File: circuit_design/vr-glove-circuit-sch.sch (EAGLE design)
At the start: 31 parts, among them U1 ARDUINO_SHIELDNO_SILK

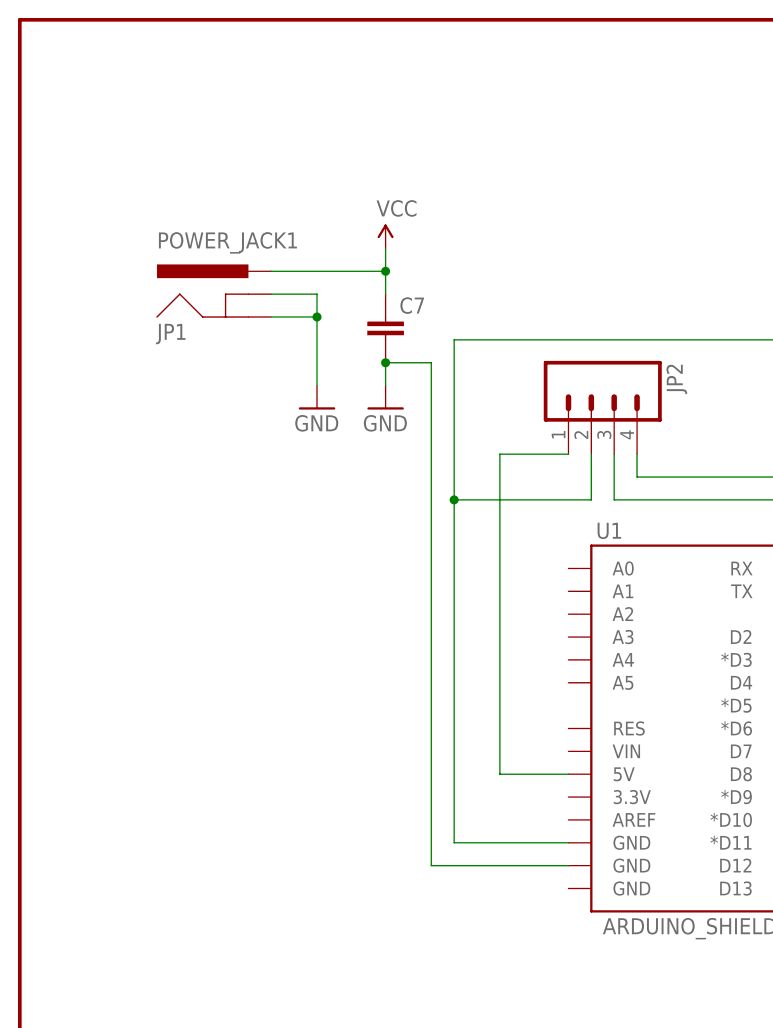
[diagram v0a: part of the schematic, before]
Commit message: added power supply
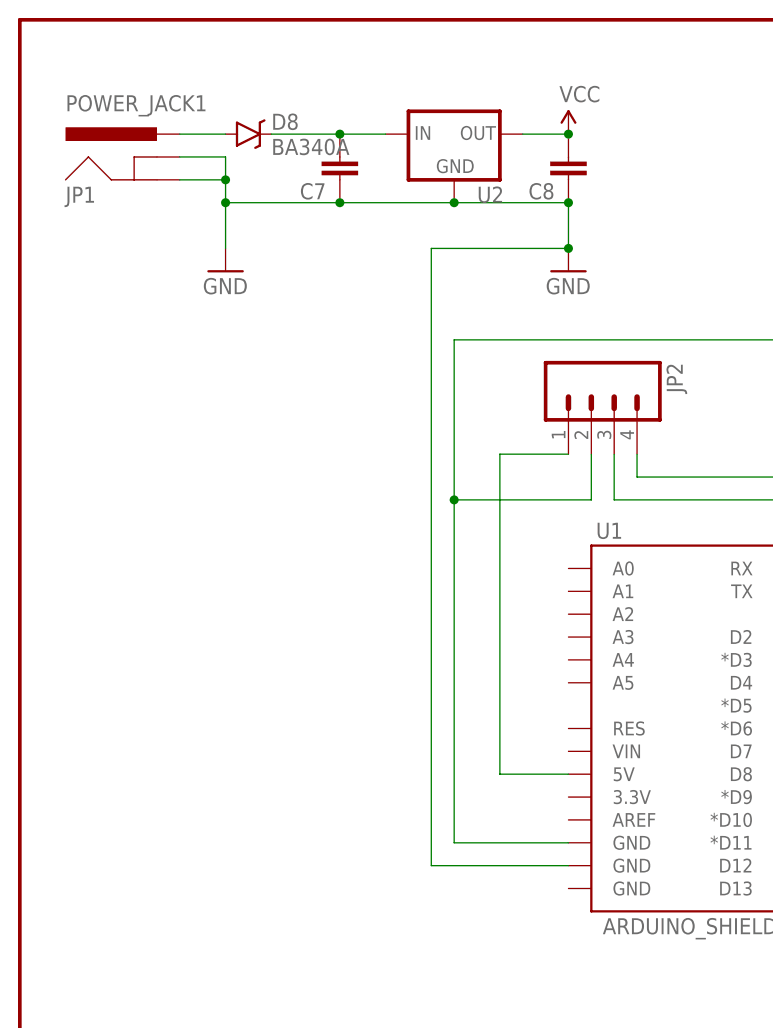
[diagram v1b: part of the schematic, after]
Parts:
- added C8: (no value), SparkFun-Capacitors:CAP0402-CAP
- added D8: BA340A, SparkFun-DiscreteSemi:B340A
- added U2: (no value), SparkFun-PowerIC:V_REG_78XXSIDE
- C7: device SparkFun-Capacitors:CAPPTH -> SparkFun-Capacitors:CAP0402-CAP
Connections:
- new net N$25: C7.2, D8.C, U2.IN
- new net N$9: D8.A, JP1.PWR
- net GND: now also C7.1, C8.1, U2.GND; no longer C7.2
- net VCC: now also C8.2, U2.OUT; no longer C7.1, JP1.PWR
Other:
- moved on the sheet: C7, JP1
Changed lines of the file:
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@@
 <part name="SUPPLY1" library="SparkFun-Aesthetics" deviceset="VCC" device=""/>
 <part name="GND2" library="SparkFun-Aesthetics" deviceset="GND" device=""/>
-<part name="C7" library="SparkFun-Capacitors" deviceset="CAP" device="PTH"/>
 <part name="SUPPLY2" library="SparkFun-Aesthetics" deviceset="VCC" device=""/>
 <part name="FRAME1" library="SparkFun-Aesthetics" deviceset="FRAME-LETTER" device=""/>
@@
 <part name="JP11" library="SparkFun-Connectors" deviceset="M06" device="SILK_FEMALE_PTH"/>
 <part name="JP2" library="SparkFun-Connectors" deviceset="M04" device="LOCK"/>
+<part name="U2" library="SparkFun-PowerIC" deviceset="V_REG_78XX" device="SIDE"/>
+<part name="C7" library="SparkFun-Capacitors" deviceset="CAP" device="0402-CAP"/>
+<part name="C8" library="SparkFun-Capacitors" deviceset="CAP" device="0402-CAP"/>
+<part name="D8" library="SparkFun-DiscreteSemi" deviceset="B340A" device="" value="BA340A"/>
 </parts>
 <sheets>
@@
 <instances>
 <instance part="U1" gate="G$1" x="12.7" y="81.28"/>
-<instance part="JP1" gate="G$1" x="-35.56" y="124.46"/>
+<instance part="JP1" gate="G$1" x="-45.72" y="139.7"/>
 <instance part="U$1" gate="G$1" x="71.12" y="116.84"/>
 <instance part="D7" gate="G$1" x="83.82" y="106.68" rot="R270"/>
@@
 <instance part="C6" gate="G$1" x="114.3" y="35.56" rot="R180"/>
 <instance part="R5" gate="G$1" x="96.52" y="43.18"/>
-<instance part="GND1" gate="1" x="-27.94" y="116.84"/>
-<instance part="SUPPLY1" gate="G$1" x="-20.32" y="134.62"/>
-<instance part="GND2" gate="1" x="-20.32" y="116.84"/>
-<instance part="C7" gate="G$1" x="-20.32" y="124.46"/>
+<instance part="GND1" gate="1" x="-38.1" y="132.08"/>
+<instance part="SUPPLY1" gate="G$1" x="0" y="147.32"/>
+<instance part="GND2" gate="1" x="0" y="132.08"/>
 <instance part="SUPPLY2" gate="G$1" x="132.08" y="119.38"/>
 <instance part="FRAME1" gate="G$1" x="-60.96" y="-25.4"/>
@@
 <instance part="JP11" gate="G$1" x="149.86" y="53.34" rot="R180"/>
 <instance part="JP2" gate="G$1" x="2.54" y="116.84" rot="R270"/>
+<instance part="U2" gate="G$1" x="-12.7" y="147.32"/>
+<instance part="C7" gate="G$1" x="-25.4" y="144.78" rot="R180"/>
+<instance part="C8" gate="G$1" x="0" y="144.78" rot="R180"/>
+<instance part="D8" gate="G$1" x="-35.56" y="147.32"/>
 </instances>
 <busses>
@@
 </net>
 <net name="VCC" class="0">
-<segment>
-<pinref part="JP1" gate="G$1" pin="PWR"/>
-<wire x1="-33.02" y1="132.08" x2="-20.32" y2="132.08" width="0.1524" layer="91"/>
-<pinref part="SUPPLY1" gate="G$1" pin="VCC"/>
-<wire x1="-20.32" y1="132.08" x2="-20.32" y2="134.62" width="0.1524" layer="91"/>
-<pinref part="C7" gate="G$1" pin="1"/>
-<wire x1="-20.32" y1="132.08" x2="-20.32" y2="129.54" width="0.1524" layer="91"/>
-<junction x="-20.32" y="132.08"/>
-</segment>
 <segment>
 <pinref part="C4" gate="G$1" pin="1"/>
@@
 <wire x1="134.62" y1="58.42" x2="144.78" y2="58.42" width="0.1524" layer="91"/>
 </segment>
-</net>
-<net name="GND" class="0">
-<segment>
-<pinref part="JP1" gate="G$1" pin="GNDBREAK"/>
-<wire x1="-33.02" y1="129.54" x2="-27.94" y2="129.54" width="0.1524" layer="91"/>
-<pinref part="GND1" gate="1" pin="GND"/>
-<wire x1="-27.94" y1="129.54" x2="-27.94" y2="127" width="0.1524" layer="91"/>
-<pinref part="JP1" gate="G$1" pin="GND"/>
-<wire x1="-27.94" y1="127" x2="-27.94" y2="119.38" width="0.1524" layer="91"/>
-<wire x1="-33.02" y1="127" x2="-27.94" y2="127" width="0.1524" layer="91"/>
-<junction x="-27.94" y="127"/>
-</segment>
-<segment>
-<pinref part="C7" gate="G$1" pin="2"/>
-<pinref part="GND2" gate="1" pin="GND"/>
-<wire x1="-20.32" y1="121.92" x2="-20.32" y2="119.38" width="0.1524" layer="91"/>
-<pinref part="U1" gate="G$1" pin="GND@1"/>
-<wire x1="0" y1="66.04" x2="-15.24" y2="66.04" width="0.1524" layer="91"/>
-<wire x1="-15.24" y1="66.04" x2="-15.24" y2="121.92" width="0.1524" layer="91"/>
-<wire x1="-15.24" y1="121.92" x2="-20.32" y2="121.92" width="0.1524" layer="91"/>
-<junction x="-20.32" y="121.92"/>
+<segment>
+<pinref part="U2" gate="G$1" pin="OUT"/>
+<pinref part="C8" gate="G$1" pin="2"/>
+<wire x1="-5.08" y1="147.32" x2="0" y2="147.32" width="0.1524" layer="91"/>
+<pinref part="SUPPLY1" gate="G$1" pin="VCC"/>
+<junction x="0" y="147.32"/>
 </segment>
 </net>
@@
 </segment>
 </net>
+<net name="N$9" class="0">
+<segment>
+<pinref part="JP1" gate="G$1" pin="PWR"/>
+<pinref part="D8" gate="G$1" pin="A"/>
+<wire x1="-43.18" y1="147.32" x2="-38.1" y2="147.32" width="0.1524" layer="91"/>
+</segment>
+</net>
+<net name="N$25" class="0">
+<segment>
+<pinref part="D8" gate="G$1" pin="C"/>
+<pinref part="C7" gate="G$1" pin="2"/>
+<wire x1="-33.02" y1="147.32" x2="-25.4" y2="147.32" width="0.1524" layer="91"/>
+<pinref part="U2" gate="G$1" pin="IN"/>
+<wire x1="-25.4" y1="147.32" x2="-20.32" y2="147.32" width="0.1524" layer="91"/>
+<junction x="-25.4" y="147.32"/>
+</segment>
+</net>
+<net name="GND" class="0">
+<segment>
+<pinref part="JP1" gate="G$1" pin="GNDBREAK"/>
+<wire x1="-43.18" y1="144.78" x2="-38.1" y2="144.78" width="0.1524" layer="91"/>
+<pinref part="GND1" gate="1" pin="GND"/>
+<wire x1="-38.1" y1="144.78" x2="-38.1" y2="142.24" width="0.1524" layer="91"/>
+<pinref part="JP1" gate="G$1" pin="GND"/>
+<wire x1="-38.1" y1="142.24" x2="-38.1" y2="139.7" width="0.1524" layer="91"/>
+<wire x1="-38.1" y1="139.7" x2="-38.1" y2="134.62" width="0.1524" layer="91"/>
+<wire x1="-43.18" y1="142.24" x2="-38.1" y2="142.24" width="0.1524" layer="91"/>
+<junction x="-38.1" y="142.24"/>
+<pinref part="C7" gate="G$1" pin="1"/>
+<wire x1="-38.1" y1="139.7" x2="-25.4" y2="139.7" width="0.1524" layer="91"/>
+<junction x="-38.1" y="139.7"/>
+<pinref part="U2" gate="G$1" pin="GND"/>
+<wire x1="-25.4" y1="139.7" x2="-12.7" y2="139.7" width="0.1524" layer="91"/>
+<junction x="-25.4" y="139.7"/>
+<pinref part="C8" gate="G$1" pin="1"/>
+<wire x1="-12.7" y1="139.7" x2="0" y2="139.7" width="0.1524" layer="91"/>
+<junction x="-12.7" y="139.7"/>
+<pinref part="GND2" gate="1" pin="GND"/>
+<wire x1="0" y1="134.62" x2="0" y2="139.7" width="0.1524" layer="91"/>
+<junction x="0" y="139.7"/>
+<pinref part="U1" gate="G$1" pin="GND@1"/>
+<wire x1="0" y1="66.04" x2="-15.24" y2="66.04" width="0.1524" layer="91"/>
+<wire x1="-15.24" y1="66.04" x2="-15.24" y2="134.62" width="0.1524" layer="91"/>
+<wire x1="-15.24" y1="134.62" x2="0" y2="134.62" width="0.1524" layer="91"/>
+<junction x="0" y="134.62"/>
+</segment>
+</net>

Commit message: finialized circuit design
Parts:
- renumbered U$1 to T1, U$2 to T2, U$3 to T3, U$4 to T4, U$5 to T5, U$6 to T6
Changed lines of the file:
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@@
 <part name="U1" library="SparkFun-Boards" deviceset="ARDUINO_SHIELD" device="NO_SILK"/>
 <part name="JP1" library="SparkFun-Connectors" deviceset="POWER_JACK" device="1"/>
-<part name="U$1" library="GeekAmmo" deviceset="N-CHANNEL-MOSFET" device="-BSS138"/>
+<part name="T1" library="GeekAmmo" deviceset="N-CHANNEL-MOSFET" device="-BSS138"/>
 <part name="D7" library="SparkFun-DiscreteSemi" deviceset="DIODE" device="SMA"/>
 <part name="C1" library="SparkFun-Capacitors" deviceset="CAP" device="PTH"/>
 <part name="R7" library="SparkFun-Resistors" deviceset="RESISTOR" device="PTH-1/2W"/>
-<part name="U$2" library="GeekAmmo" deviceset="N-CHANNEL-MOSFET" device="-BSS138"/>
+<part name="T2" library="GeekAmmo" deviceset="N-CHANNEL-MOSFET" device="-BSS138"/>
 <part name="D1" library="SparkFun-DiscreteSemi" deviceset="DIODE" device="SMA"/>
 <part name="C2" library="SparkFun-Capacitors" deviceset="CAP" device="PTH"/>
 <part name="R1" library="SparkFun-Resistors" deviceset="RESISTOR" device="PTH-1/2W"/>
-<part name="U$3" library="GeekAmmo" deviceset="N-CHANNEL-MOSFET" device="-BSS138"/>
+<part name="T3" library="GeekAmmo" deviceset="N-CHANNEL-MOSFET" device="-BSS138"/>
 <part name="D2" library="SparkFun-DiscreteSemi" deviceset="DIODE" device="SMA"/>
 <part name="C3" library="SparkFun-Capacitors" deviceset="CAP" device="PTH"/>
 <part name="R2" library="SparkFun-Resistors" deviceset="RESISTOR" device="PTH-1/2W"/>
-<part name="U$4" library="GeekAmmo" deviceset="N-CHANNEL-MOSFET" device="-BSS138"/>
+<part name="T4" library="GeekAmmo" deviceset="N-CHANNEL-MOSFET" device="-BSS138"/>
 <part name="D3" library="SparkFun-DiscreteSemi" deviceset="DIODE" device="SMA"/>
 <part name="C4" library="SparkFun-Capacitors" deviceset="CAP" device="PTH"/>
 <part name="R3" library="SparkFun-Resistors" deviceset="RESISTOR" device="PTH-1/2W"/>
-<part name="U$5" library="GeekAmmo" deviceset="N-CHANNEL-MOSFET" device="-BSS138"/>
+<part name="T5" library="GeekAmmo" deviceset="N-CHANNEL-MOSFET" device="-BSS138"/>
 <part name="D4" library="SparkFun-DiscreteSemi" deviceset="DIODE" device="SMA"/>
 <part name="C5" library="SparkFun-Capacitors" deviceset="CAP" device="PTH"/>
 <part name="R4" library="SparkFun-Resistors" deviceset="RESISTOR" device="PTH-1/2W"/>
-<part name="U$6" library="GeekAmmo" deviceset="N-CHANNEL-MOSFET" device="-BSS138"/>
+<part name="T6" library="GeekAmmo" deviceset="N-CHANNEL-MOSFET" device="-BSS138"/>
 <part name="D5" library="SparkFun-DiscreteSemi" deviceset="DIODE" device="SMA"/>
 <part name="C6" library="SparkFun-Capacitors" deviceset="CAP" device="PTH"/>
@@
 <instance part="U1" gate="G$1" x="12.7" y="81.28"/>
 <instance part="JP1" gate="G$1" x="-45.72" y="139.7"/>
-<instance part="U$1" gate="G$1" x="71.12" y="116.84"/>
+<instance part="T1" gate="G$1" x="71.12" y="116.84"/>
 <instance part="D7" gate="G$1" x="83.82" y="106.68" rot="R270"/>
 <instance part="C1" gate="G$1" x="76.2" y="106.68" rot="R180"/>
 <instance part="R7" gate="G$1" x="58.42" y="114.3"/>
-<instance part="U$2" gate="G$1" x="71.12" y="88.9"/>
+<instance part="T2" gate="G$1" x="71.12" y="88.9"/>
 <instance part="D1" gate="G$1" x="83.82" y="78.74" rot="R270"/>
 <instance part="C2" gate="G$1" x="76.2" y="78.74" rot="R180"/>
 <instance part="R1" gate="G$1" x="58.42" y="86.36"/>
-<instance part="U$3" gate="G$1" x="73.66" y="60.96"/>
+<instance part="T3" gate="G$1" x="73.66" y="60.96"/>
 <instance part="D2" gate="G$1" x="86.36" y="50.8" rot="R270"/>
 <instance part="C3" gate="G$1" x="78.74" y="50.8" rot="R180"/>
 <instance part="R2" gate="G$1" x="60.96" y="58.42"/>
-<instance part="U$4" gate="G$1" x="109.22" y="101.6"/>
+<instance part="T4" gate="G$1" x="109.22" y="101.6"/>
 <instance part="D3" gate="G$1" x="121.92" y="91.44" rot="R270"/>
 <instance part="C4" gate="G$1" x="114.3" y="91.44" rot="R180"/>
 <instance part="R3" gate="G$1" x="96.52" y="99.06"/>
-<instance part="U$5" gate="G$1" x="109.22" y="73.66"/>
+<instance part="T5" gate="G$1" x="109.22" y="73.66"/>
 <instance part="D4" gate="G$1" x="121.92" y="63.5" rot="R270"/>
 <instance part="C5" gate="G$1" x="114.3" y="63.5" rot="R180"/>
 <instance part="R4" gate="G$1" x="96.52" y="71.12"/>
-<instance part="U$6" gate="G$1" x="109.22" y="45.72"/>
+<instance part="T6" gate="G$1" x="109.22" y="45.72"/>
 <instance part="D5" gate="G$1" x="121.92" y="35.56" rot="R270"/>
 <instance part="C6" gate="G$1" x="114.3" y="35.56" rot="R180"/>
@@
 <segment>
 <pinref part="R7" gate="G$1" pin="2"/>
-<pinref part="U$1" gate="G$1" pin="G"/>
+<pinref part="T1" gate="G$1" pin="G"/>
 <wire x1="63.5" y1="114.3" x2="66.04" y2="114.3" width="0.1524" layer="91"/>
 </segment>
@@
 <pinref part="C1" gate="G$1" pin="2"/>
 <wire x1="83.82" y1="109.22" x2="76.2" y2="109.22" width="0.1524" layer="91"/>
-<pinref part="U$1" gate="G$1" pin="S"/>
+<pinref part="T1" gate="G$1" pin="S"/>
 <wire x1="76.2" y1="109.22" x2="73.66" y2="109.22" width="0.1524" layer="91"/>
 <junction x="76.2" y="109.22"/>
@@
 <segment>
 <pinref part="R1" gate="G$1" pin="2"/>
-<pinref part="U$2" gate="G$1" pin="G"/>
+<pinref part="T2" gate="G$1" pin="G"/>
 <wire x1="63.5" y1="86.36" x2="66.04" y2="86.36" width="0.1524" layer="91"/>
 </segment>
@@
 <pinref part="C2" gate="G$1" pin="2"/>
 <wire x1="83.82" y1="81.28" x2="76.2" y2="81.28" width="0.1524" layer="91"/>
-<pinref part="U$2" gate="G$1" pin="S"/>
+<pinref part="T2" gate="G$1" pin="S"/>
 <wire x1="76.2" y1="81.28" x2="73.66" y2="81.28" width="0.1524" layer="91"/>
 <junction x="76.2" y="81.28"/>
@@
 <segment>
 <pinref part="R2" gate="G$1" pin="2"/>
-<pinref part="U$3" gate="G$1" pin="G"/>
+<pinref part="T3" gate="G$1" pin="G"/>
 <wire x1="66.04" y1="58.42" x2="68.58" y2="58.42" width="0.1524" layer="91"/>
 </segment>
@@
 <pinref part="C3" gate="G$1" pin="2"/>
 <wire x1="86.36" y1="53.34" x2="78.74" y2="53.34" width="0.1524" layer="91"/>
-<pinref part="U$3" gate="G$1" pin="S"/>
+<pinref part="T3" gate="G$1" pin="S"/>
 <wire x1="78.74" y1="53.34" x2="76.2" y2="53.34" width="0.1524" layer="91"/>
 <junction x="78.74" y="53.34"/>
@@
 <segment>
 <pinref part="R3" gate="G$1" pin="2"/>
-<pinref part="U$4" gate="G$1" pin="G"/>
+<pinref part="T4" gate="G$1" pin="G"/>
 <wire x1="101.6" y1="99.06" x2="104.14" y2="99.06" width="0.1524" layer="91"/>
 </segment>
@@
 <pinref part="C4" gate="G$1" pin="2"/>
 <wire x1="121.92" y1="93.98" x2="114.3" y2="93.98" width="0.1524" layer="91"/>
-<pinref part="U$4" gate="G$1" pin="S"/>
+<pinref part="T4" gate="G$1" pin="S"/>
 <wire x1="114.3" y1="93.98" x2="111.76" y2="93.98" width="0.1524" layer="91"/>
 <junction x="114.3" y="93.98"/>
@@
 <segment>
 <pinref part="R4" gate="G$1" pin="2"/>
-<pinref part="U$5" gate="G$1" pin="G"/>
+<pinref part="T5" gate="G$1" pin="G"/>
 <wire x1="101.6" y1="71.12" x2="104.14" y2="71.12" width="0.1524" layer="91"/>
 </segment>
@@
 <pinref part="C5" gate="G$1" pin="2"/>
 <wire x1="121.92" y1="66.04" x2="114.3" y2="66.04" width="0.1524" layer="91"/>
-<pinref part="U$5" gate="G$1" pin="S"/>
+<pinref part="T5" gate="G$1" pin="S"/>
 <wire x1="114.3" y1="66.04" x2="111.76" y2="66.04" width="0.1524" layer="91"/>
 <junction x="114.3" y="66.04"/>
@@
 <segment>
 <pinref part="R5" gate="G$1" pin="2"/>
-<pinref part="U$6" gate="G$1" pin="G"/>
+<pinref part="T6" gate="G$1" pin="G"/>
 <wire x1="101.6" y1="43.18" x2="104.14" y2="43.18" width="0.1524" layer="91"/>
 </segment>
@@
 <pinref part="C6" gate="G$1" pin="2"/>
 <wire x1="121.92" y1="38.1" x2="114.3" y2="38.1" width="0.1524" layer="91"/>
-<pinref part="U$6" gate="G$1" pin="S"/>
+<pinref part="T6" gate="G$1" pin="S"/>
 <wire x1="114.3" y1="38.1" x2="111.76" y2="38.1" width="0.1524" layer="91"/>
 <junction x="114.3" y="38.1"/>
@@
 <net name="N$3" class="0">
 <segment>
-<pinref part="U$1" gate="G$1" pin="D"/>
+<pinref part="T1" gate="G$1" pin="D"/>
 <wire x1="73.66" y1="124.46" x2="53.34" y2="124.46" width="0.1524" layer="91"/>
 <wire x1="53.34" y1="124.46" x2="50.8" y2="124.46" width="0.1524" layer="91"/>
@@
 <wire x1="-12.7" y1="106.68" x2="-12.7" y2="68.58" width="0.1524" layer="91"/>
 <wire x1="-12.7" y1="68.58" x2="0" y2="68.58" width="0.1524" layer="91"/>
-<pinref part="U$2" gate="G$1" pin="D"/>
+<pinref part="T2" gate="G$1" pin="D"/>
 <wire x1="73.66" y1="96.52" x2="45.72" y2="96.52" width="0.1524" layer="91"/>
 <wire x1="45.72" y1="96.52" x2="45.72" y2="124.46" width="0.1524" layer="91"/>
 <junction x="45.72" y="124.46"/>
-<pinref part="U$4" gate="G$1" pin="D"/>
+<pinref part="T4" gate="G$1" pin="D"/>
 <wire x1="111.76" y1="109.22" x2="111.76" y2="127" width="0.1524" layer="91"/>
 <wire x1="111.76" y1="127" x2="53.34" y2="127" width="0.1524" layer="91"/>
 <wire x1="53.34" y1="127" x2="53.34" y2="124.46" width="0.1524" layer="91"/>
 <junction x="53.34" y="124.46"/>
-<pinref part="U$3" gate="G$1" pin="D"/>
+<pinref part="T3" gate="G$1" pin="D"/>
 <wire x1="76.2" y1="68.58" x2="48.26" y2="68.58" width="0.1524" layer="91"/>
 <wire x1="48.26" y1="68.58" x2="48.26" y2="124.46" width="0.1524" layer="91"/>
 <junction x="48.26" y="124.46"/>
-<pinref part="U$5" gate="G$1" pin="D"/>
+<pinref part="T5" gate="G$1" pin="D"/>
 <wire x1="111.76" y1="81.28" x2="50.8" y2="83.82" width="0.1524" layer="91"/>
 <wire x1="50.8" y1="83.82" x2="50.8" y2="124.46" width="0.1524" layer="91"/>
 <junction x="50.8" y="124.46"/>
-<pinref part="U$6" gate="G$1" pin="D"/>
+<pinref part="T6" gate="G$1" pin="D"/>
 <wire x1="111.76" y1="53.34" x2="43.18" y2="55.88" width="0.1524" layer="91"/>
 <wire x1="43.18" y1="55.88" x2="43.18" y2="124.46" width="0.1524" layer="91"/>
